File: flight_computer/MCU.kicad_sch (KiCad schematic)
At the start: 22 parts, among them J1 Conn_02x05_Counter_Clockwise, J2 MEM2061-01-188-00-A_REVA, Q1 Q_NPN_BEC, SW1 SW_Push, SW2 SW_Push, U2 STM8S007C8T6, Y1 12MHz

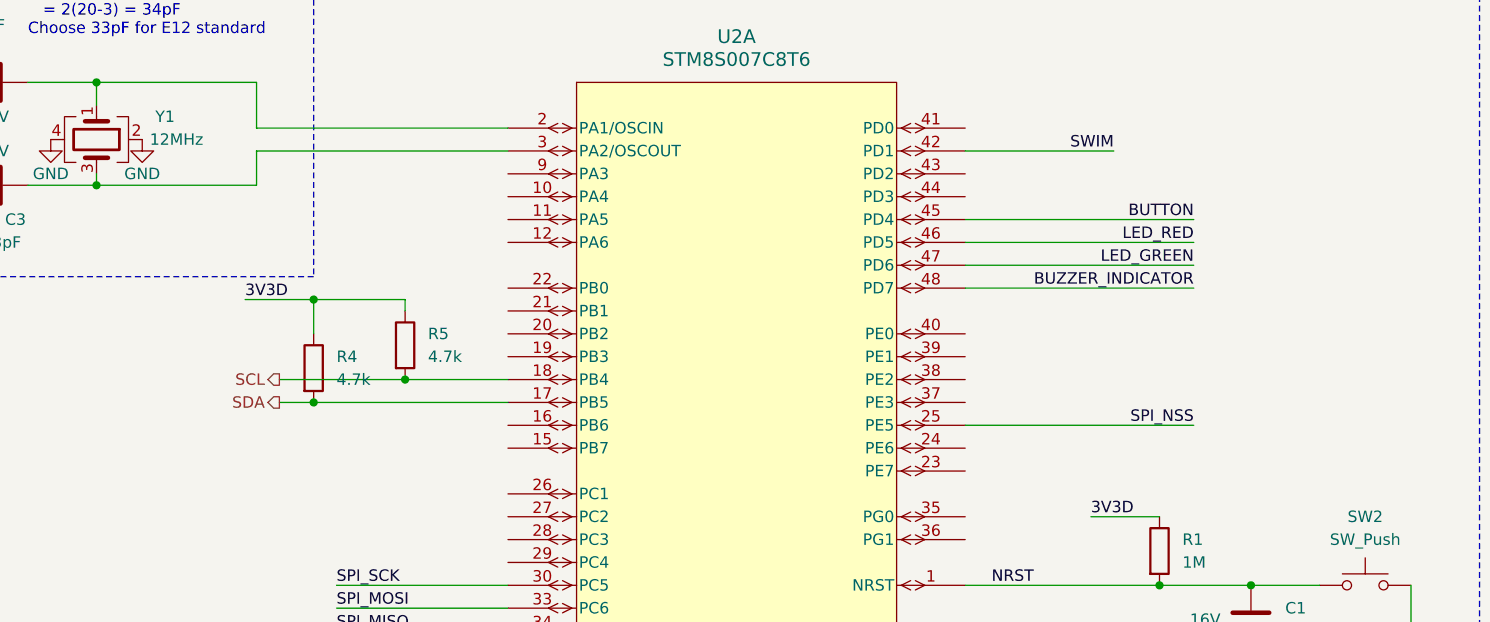
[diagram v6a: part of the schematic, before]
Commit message: Finishing gps, ready to connect all
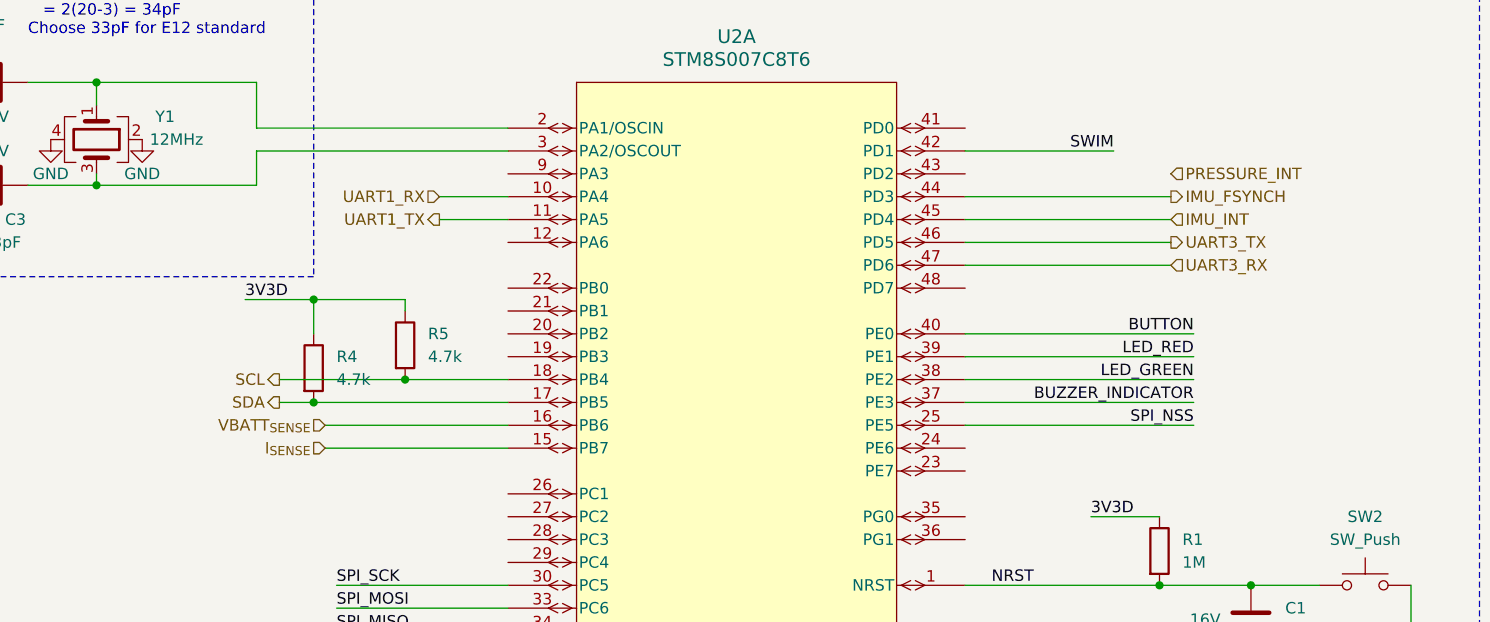
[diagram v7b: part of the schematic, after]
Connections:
- net BUTTON: now also U2.40 (PE0); no longer U2.45 (PD4)
- net BUZZER_INDICATOR: now also U2.37 (PE3); no longer U2.48 (PD7)
- net LED_GREEN: now also U2.38 (PE2); no longer U2.47 (PD6)
- net LED_RED: now also U2.39 (PE1); no longer U2.46 (PD5)
- net UART1_RX: now reaches U2.10 (PA4)
- net UART1_TX: now reaches U2.11 (PA5)
- net I_{SENSE}: now reaches U2.15 (PB7)
- net VBATT_{SENSE}: now reaches U2.16 (PB6)
- net IMU_FSYNCH: now reaches U2.44 (PD3)
- new net IMU_INT: U2.45 (PD4)
- new net UART3_RX: U2.47 (PD6)
- new net UART3_TX: U2.46 (PD5)
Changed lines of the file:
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@@
+    (stroke (width 0) (type default))
+  )
+  (wire (pts (xy 203.2 130.81) (xy 210.82 130.81))
     (stroke (width 0) (type default))
   )
@@
     (stroke (width 0) (type default))
   )
-  (wire (pts (xy 261.62 135.89) (xy 287.02 135.89))
-    (stroke (width 0) (type default))
-  )
-  (wire (pts (xy 261.62 133.35) (xy 287.02 133.35))
+  (wire (pts (xy 261.62 148.59) (xy 287.02 148.59))
+    (stroke (width 0) (type default))
+  )
+  (wire (pts (xy 261.62 146.05) (xy 287.02 146.05))
     (stroke (width 0) (type default))
   )
@@
     (stroke (width 0) (type default))
   )
+  (wire (pts (xy 190.5 156.21) (xy 210.82 156.21))
+    (stroke (width 0) (type default))
+  )
+  (wire (pts (xy 203.2 128.27) (xy 210.82 128.27))
+    (stroke (width 0) (type default))
+  )
   (wire (pts (xy 210.82 123.19) (xy 182.88 123.19))
     (stroke (width 0) (type default))
@@
     (stroke (width 0) (type default))
   )
+  (wire (pts (xy 261.62 130.81) (xy 284.48 130.81))
+    (stroke (width 0) (type default))
+  )
   (wire (pts (xy 165.1 115.57) (xy 165.1 118.11))
     (stroke (width 0) (type default))
@@
     (stroke (width 0) (type default))
   )
+  (wire (pts (xy 261.62 128.27) (xy 284.48 128.27))
+    (stroke (width 0) (type default))
+  )
   (wire (pts (xy 59.69 185.42) (xy 78.74 185.42))
     (stroke (width 0) (type default))
@@
     (stroke (width 0) (type default))
   )
-  (wire (pts (xy 261.62 138.43) (xy 287.02 138.43))
+  (wire (pts (xy 261.62 151.13) (xy 287.02 151.13))
     (stroke (width 0) (type default))
   )
@@
     (stroke (width 0) (type default))
   )
+  (wire (pts (xy 261.62 135.89) (xy 284.48 135.89))
+    (stroke (width 0) (type default))
+  )
   (wire (pts (xy 63.5 128.27) (xy 68.58 128.27))
     (stroke (width 0) (type default))
@@
     (stroke (width 0) (type default))
   )
-  (wire (pts (xy 261.62 130.81) (xy 287.02 130.81))
+  (wire (pts (xy 261.62 143.51) (xy 287.02 143.51))
     (stroke (width 0) (type default))
   )
@@
     (stroke (width 0) (type default))
   )
+  (wire (pts (xy 190.5 153.67) (xy 210.82 153.67))
+    (stroke (width 0) (type default))
+  )
   (wire (pts (xy 355.6 45.72) (xy 370.84 45.72))
     (stroke (width 0) (type default))
@@
   )
   (wire (pts (xy 261.62 153.67) (xy 287.02 153.67))
+    (stroke (width 0) (type default))
+  )
+  (wire (pts (xy 261.62 133.35) (xy 284.48 133.35))
     (stroke (width 0) (type default))
   )
@@
     (effects (font (size 1.27 1.27)) (justify left bottom))
   )
-  (label "LED_GREEN" (at 287.02 135.89 180) (fields_autoplaced)
-    (effects (font (size 1.27 1.27)) (justify right bottom))
-  )
-  (label "BUTTON" (at 287.02 130.81 180) (fields_autoplaced)
+  (label "LED_GREEN" (at 287.02 148.59 180) (fields_autoplaced)
+    (effects (font (size 1.27 1.27)) (justify right bottom))
+  )
+  (label "BUTTON" (at 287.02 143.51 180) (fields_autoplaced)
     (effects (font (size 1.27 1.27)) (justify right bottom))
   )
@@
     (effects (font (size 1.27 1.27)) (justify left bottom))
   )
-  (label "BUZZER_INDICATOR" (at 287.02 138.43 180) (fields_autoplaced)
+  (label "BUZZER_INDICATOR" (at 287.02 151.13 180) (fields_autoplaced)
     (effects (font (size 1.27 1.27)) (justify right bottom))
   )
@@
     (effects (font (size 1.27 1.27)) (justify left bottom))
   )
-  (label "LED_RED" (at 287.02 133.35 180) (fields_autoplaced)
+  (label "LED_RED" (at 287.02 146.05 180) (fields_autoplaced)
     (effects (font (size 1.27 1.27)) (justify right bottom))
   )
@@
     (effects (font (size 1.27 1.27)) (justify left bottom))
   )
+  (hierarchical_label "IMU_FSYNCH" (shape output) (at 284.48 128.27 0) (fields_autoplaced)
+    (effects (font (size 1.27 1.27)) (justify left))
+  )
+  (hierarchical_label "UART3_RX" (shape input) (at 284.48 135.89 0) (fields_autoplaced)
+    (effects (font (size 1.27 1.27)) (justify left))
+  )
   (hierarchical_label "3V3D" (shape input) (at 34.29 38.1 180) (fields_autoplaced)
     (effects (font (size 1.27 1.27)) (justify right))
   )
+  (hierarchical_label "I_{SENSE}" (shape input) (at 190.5 156.21 180) (fields_autoplaced)
+    (effects (font (size 1.27 1.27)) (justify right))
+  )
+  (hierarchical_label "UART1_TX" (shape output) (at 203.2 130.81 180) (fields_autoplaced)
+    (effects (font (size 1.27 1.27)) (justify right))
+  )
+  (hierarchical_label "PRESSURE_INT" (shape input) (at 284.48 125.73 0) (fields_autoplaced)
+    (effects (font (size 1.27 1.27)) (justify left))
+  )
+  (hierarchical_label "VBATT_{SENSE}" (shape input) (at 190.5 153.67 180) (fields_autoplaced)
+    (effects (font (size 1.27 1.27)) (justify right))
+  )
+  (hierarchical_label "UART3_TX" (shape output) (at 284.48 133.35 0) (fields_autoplaced)
+    (effects (font (size 1.27 1.27)) (justify left))
+  )
   (hierarchical_label "GND" (shape input) (at 34.29 68.58 180) (fields_autoplaced)
     (effects (font (size 1.27 1.27)) (justify right))
   )
+  (hierarchical_label "IMU_INT" (shape input) (at 284.48 130.81 0) (fields_autoplaced)
+    (effects (font (size 1.27 1.27)) (justify left))
+  )
   (hierarchical_label "SCL" (shape output) (at 185.42 148.59 180) (fields_autoplaced)
     (effects (font (size 1.27 1.27)) (justify right))
@@
     (effects (font (size 1.27 1.27)) (justify right))
   )
+  (hierarchical_label "UART1_RX" (shape input) (at 203.2 128.27 180) (fields_autoplaced)
+    (effects (font (size 1.27 1.27)) (justify right))
+  )

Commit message: Schematic connecting
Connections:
- net PRESSURE_INT: now also U2.43 (PD2)
- net RADIO_M1: now reaches U2.28 (PC3)
- net RADIO_M0: now reaches U2.29 (PC4)
- net IMU_FSYNCH renamed IMU_FSYNC
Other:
- note added: "Bullfrog: Testpoints :)"
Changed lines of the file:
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@@
 (kicad_sch (version 20230121) (generator eeschema)
   (paper "A3")
+  (bus_alias "I2C" (members "SDA" "SCL"))
   (junction (at 44.45 68.58) (diameter 0) (color 0 0 0 0)
   )
@@
   (no_connect (at 33.02 190.5))
   (no_connect (at 370.84 38.1))
+  (bus_entry (at 175.26 146.05) (size 2.54 2.54)
+    (stroke (width 0) (type default))
+  )
+  (bus_entry (at 175.26 148.59) (size 2.54 2.54)
+    (stroke (width 0) (type default))
+  )
   (wire (pts (xy 68.58 128.27) (xy 68.58 140.97))
     (stroke (width 0) (type default))
@@
     (stroke (width 0) (type default))
   )
+  (bus (pts (xy 175.26 146.05) (xy 175.26 148.59))
+    (stroke (width 0) (type default))
+  )
   (wire (pts (xy 29.21 101.6) (xy 57.15 101.6))
     (stroke (width 0) (type default))
   )
-  (wire (pts (xy 185.42 151.13) (xy 189.23 151.13))
+  (wire (pts (xy 177.8 151.13) (xy 189.23 151.13))
     (stroke (width 0) (type default))
   )
@@
     (stroke (width 0) (type default))
   )
+  (bus (pts (xy 175.26 143.51) (xy 175.26 146.05))
+    (stroke (width 0) (type default))
+  )
   (wire (pts (xy 355.6 48.26) (xy 370.84 48.26))
     (stroke (width 0) (type default))
@@
     (stroke (width 0) (type default))
   )
+  (wire (pts (xy 191.77 166.37) (xy 210.82 166.37))
+    (stroke (width 0) (type default))
+  )
   (wire (pts (xy 355.6 33.02) (xy 370.84 33.02))
     (stroke (width 0) (type default))
@@
     (stroke (width 0) (type default))
   )
+  (wire (pts (xy 261.62 125.73) (xy 284.48 125.73))
+    (stroke (width 0) (type default))
+  )
   (wire (pts (xy 355.6 60.96) (xy 355.6 63.5))
     (stroke (width 0) (type default))
@@
     (stroke (width 0) (type default))
   )
+  (bus (pts (xy 166.37 143.51) (xy 175.26 143.51))
+    (stroke (width 0) (type default))
+  )
   (wire (pts (xy 33.02 180.34) (xy 46.99 180.34))
     (stroke (width 0) (type default))
@@
     (stroke (width 0) (type default))
   )
-  (wire (pts (xy 185.42 148.59) (xy 199.39 148.59))
+  (wire (pts (xy 177.8 148.59) (xy 199.39 148.59))
     (stroke (width 0) (type default))
   )
   (wire (pts (xy 365.76 232.41) (xy 369.57 232.41))
+    (stroke (width 0) (type default))
+  )
+  (wire (pts (xy 191.77 168.91) (xy 210.82 168.91))
     (stroke (width 0) (type default))
   )
@@
     (effects (font (size 2 2) (thickness 0.4) bold) (justify left bottom))
   )
+  (text "Bullfrog: Testpoints :)" (at 231.14 62.23 0)
+    (effects (font (size 1.27 1.27)) (justify left bottom))
+  )
   (text "SD Card" (at 365.76 25.4 0)
     (effects (font (size 2 2) (thickness 0.4) bold) (justify left bottom))
@@
     (effects (font (size 1.27 1.27)) (justify left bottom))
   )
+  (label "SCL" (at 181.61 148.59 0)
+    (effects (font (size 1.27 1.27)) (justify left bottom))
+  )
   (label "SPI_MISO" (at 191.77 176.53 0) (fields_autoplaced)
     (effects (font (size 1.27 1.27)) (justify left bottom))
@@
     (effects (font (size 1.27 1.27)) (justify left bottom))
   )
+  (label "SDA" (at 181.61 151.13 0)
+    (effects (font (size 1.27 1.27)) (justify left bottom))
+  )
   (label "LED_RED" (at 29.21 140.97 0) (fields_autoplaced)
     (effects (font (size 1.27 1.27)) (justify left bottom))
@@
     (effects (font (size 1.27 1.27)) (justify left bottom))
   )
-  (hierarchical_label "IMU_FSYNCH" (shape output) (at 284.48 128.27 0) (fields_autoplaced)
+  (hierarchical_label "{I2C}" (shape input) (at 166.37 143.51 180) (fields_autoplaced)
+    (effects (font (size 1.27 1.27) (thickness 0.254) bold) (justify right))
+  )
+  (hierarchical_label "IMU_FSYNC" (shape output) (at 284.48 128.27 0) (fields_autoplaced)
     (effects (font (size 1.27 1.27)) (justify left))
   )
@@
     (effects (font (size 1.27 1.27)) (justify left))
   )
-  (hierarchical_label "SCL" (shape output) (at 185.42 148.59 180) (fields_autoplaced)
+  (hierarchical_label "RADIO_M0" (shape output) (at 191.77 168.91 180) (fields_autoplaced)
     (effects (font (size 1.27 1.27)) (justify right))
   )
-  (hierarchical_label "SDA" (shape output) (at 185.42 151.13 180) (fields_autoplaced)
+  (hierarchical_label "RADIO_M1" (shape output) (at 191.77 166.37 180) (fields_autoplaced)
     (effects (font (size 1.27 1.27)) (justify right))
   )
